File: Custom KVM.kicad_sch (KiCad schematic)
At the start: 2 parts, among them J1 E9320-001-01, J6 USB_A_Stacked

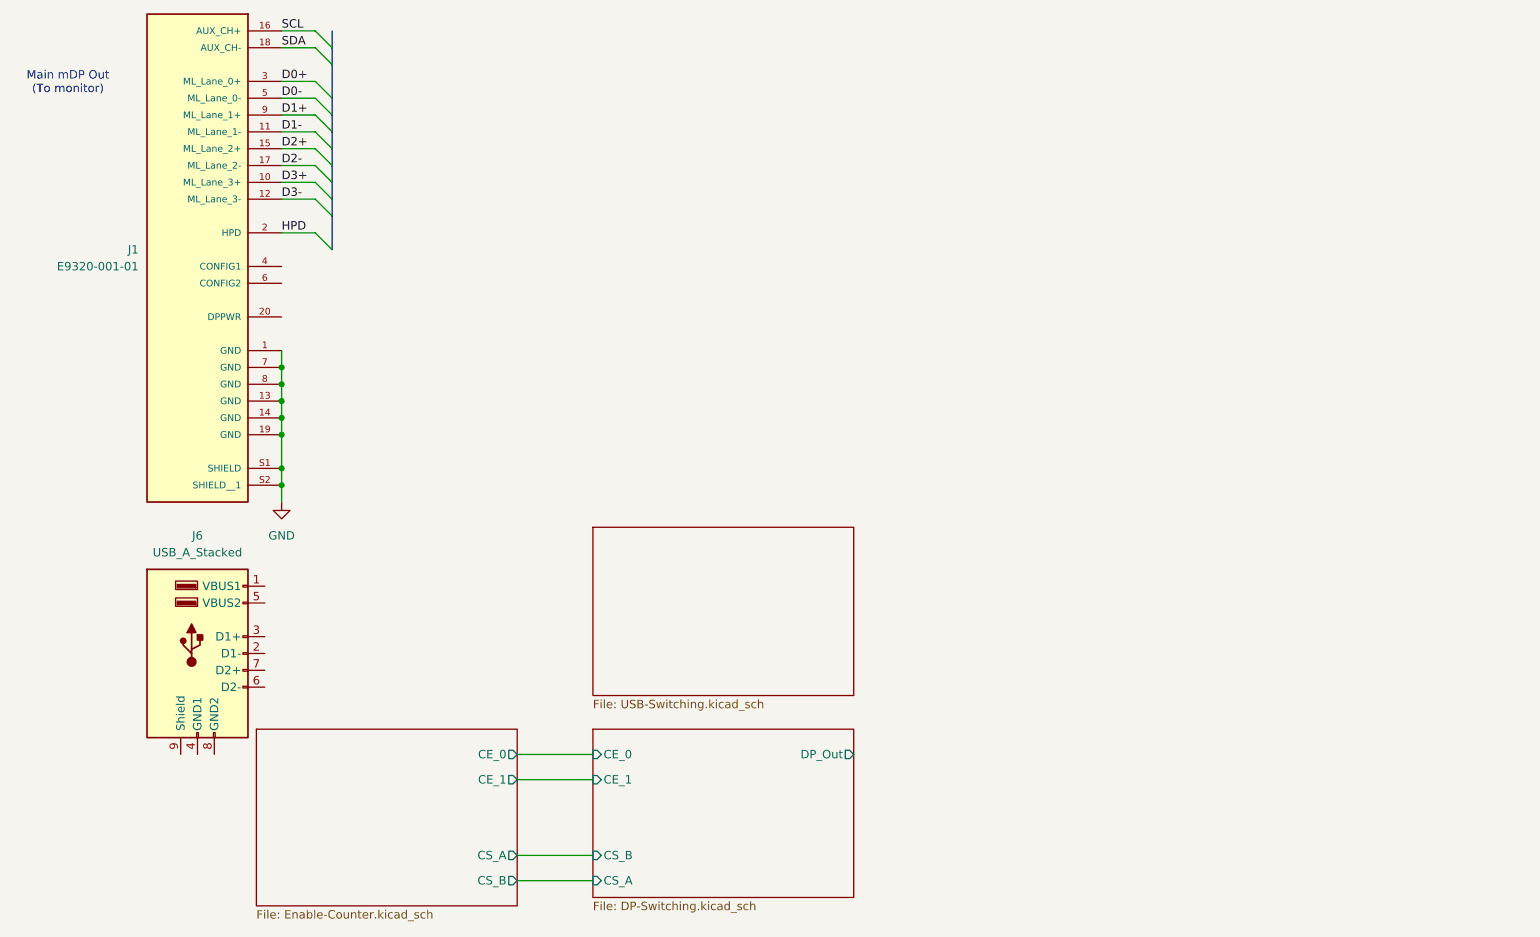
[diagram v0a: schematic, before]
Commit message: Add titles, dates, and company
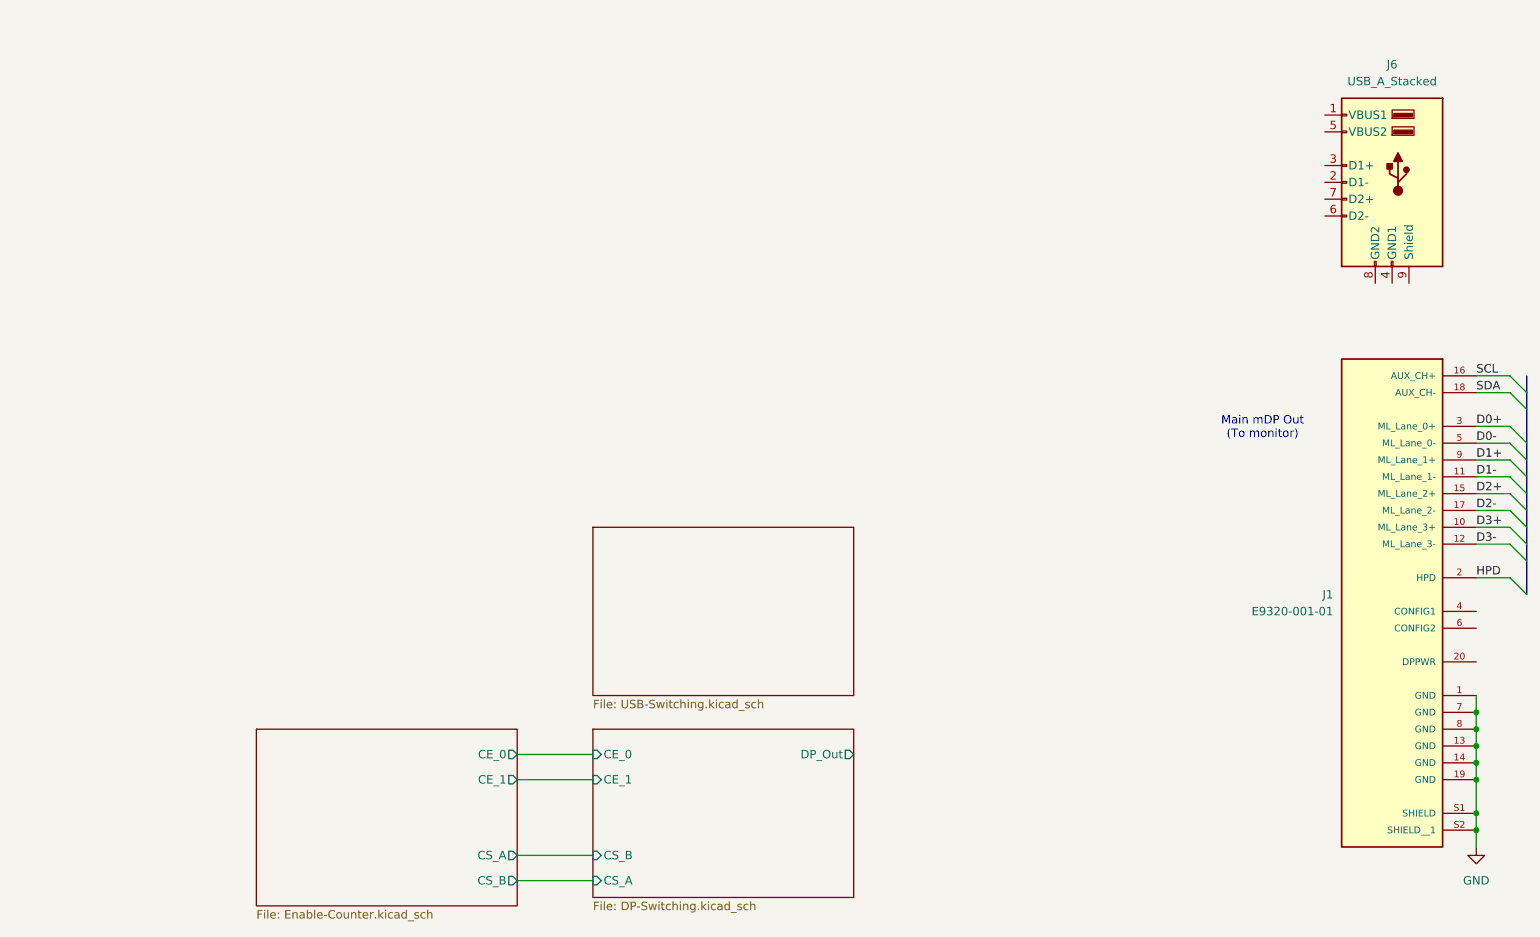
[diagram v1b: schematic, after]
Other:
- moved on the sheet: J1, J6
